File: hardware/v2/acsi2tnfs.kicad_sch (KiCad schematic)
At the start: 24 parts, among them J1 Debug, J2 To ACSI, J3 To SD card, J4 Debug Header, Q1 BC547, Q2 BC547, U1 SN74LVC245APW, U2 SN74LVC245APW

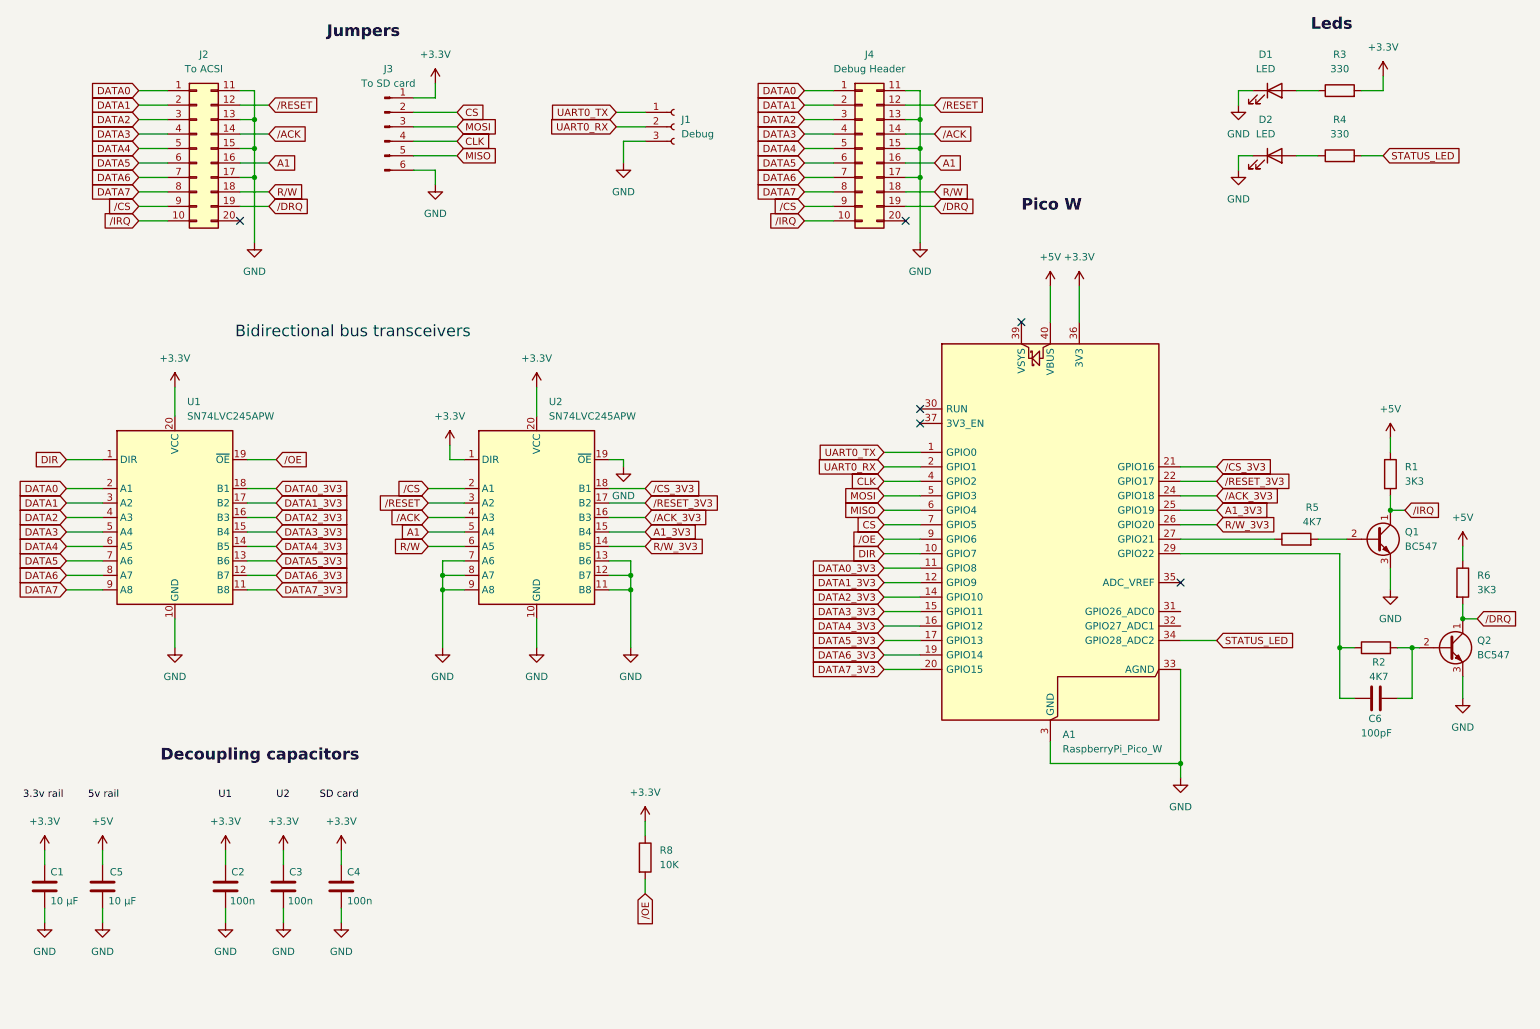
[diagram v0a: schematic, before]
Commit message: Hardware: v2 board (DB19 on the PCB, 74LS07, SD, button, leds) and dev schematic changes
Co-Authored-By: Claude Opus 5.5 <noreply@anthropic.com>
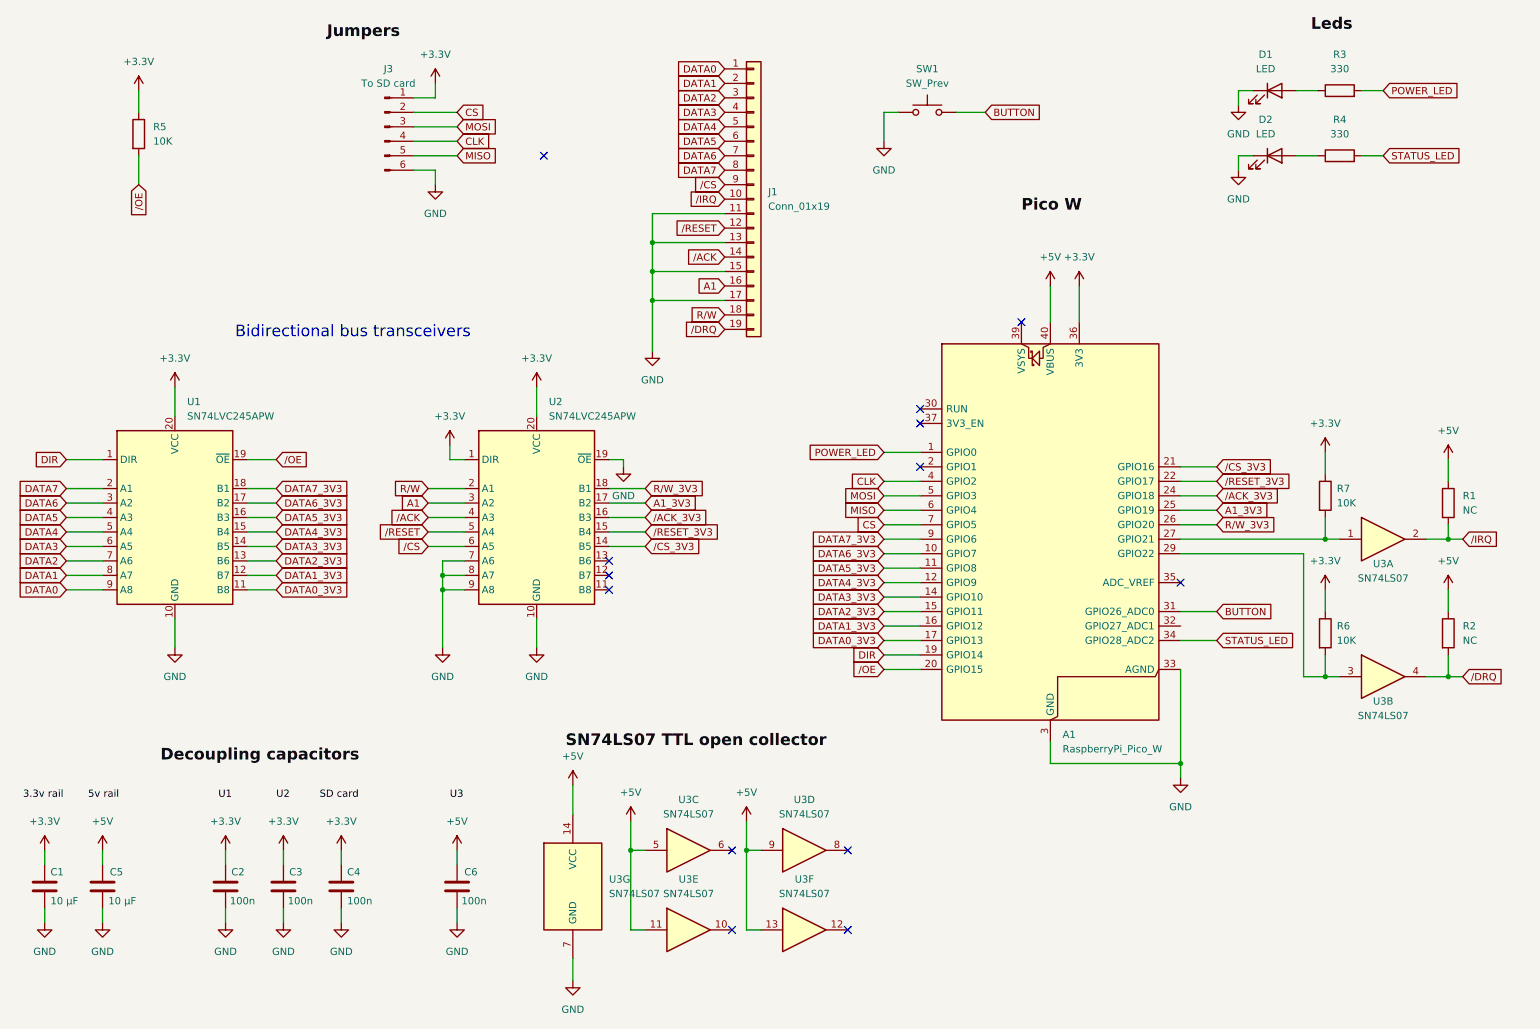
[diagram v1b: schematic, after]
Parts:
- removed J1: Debug, Connector_PinHeader_2.54mm:PinHeader_1x03_P2.54mm_Vertical, symbol Connector:Conn_01x03_Socket
- removed J2: To ACSI, Library:PinHeader_2x10_P2.54mm_Vertical_NR_PER_ROW, symbol Connector_Generic:Conn_02x10_Top_Bottom
- removed J4: Debug Header, Library:PinHeader_2x10_P2.54mm_Vertical_NR_PER_ROW, symbol Connector_Generic:Conn_02x10_Top_Bottom
- removed Q1, Q2: BC547, Package_TO_SOT_THT:TO-92_Inline, symbol Transistor_BJT:BC547
- removed R8: 10K, Resistor_SMD:R_0805_2012Metric, symbol Device:R
- added J1: Conn_01x19, ACSI Connector:ACSI_DB19_Male_WAGO_243-131, symbol Connector_Generic:Conn_01x19
- added R7: 10K, Resistor_SMD:R_0805_2012Metric, symbol Device:R
- added SW1: SW_Prev, Button_Switch_THT:SW_Tactile_SKHH_Angled, symbol Switch:SW_Push
- added U3: SN74LS07, Package_SO:SOIC-14_3.9x8.7mm_P1.27mm, symbol 74xx:SN74LS07
- C6: value 100pF -> 100n
- R1: value 3K3 -> NC
- R2: value 4K7 -> NC
- R5: value 4K7 -> 10K
- R6: value 3K3 -> 10K
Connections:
- net +3.3V: now also R5.1, R6.1, R7.1; no longer R3.2
- net +5V: now also C6.1, R2.1, U3.11, U3.13, U3.14 (VCC), U3.5, U3.9; no longer R6.1
- net A1: now also U2.3 (A2), J1.16 (Pin_16); no longer U2.5 (A4)
- net A1_3V3: now also U2.17 (B2); no longer U2.15 (B4)
- net DATA0: now also U1.9 (A8), J1.1 (Pin_1); no longer U1.2 (A1)
- net DATA0_3V3: now also A1.17 (GPIO13), U1.11 (B8); no longer A1.11 (GPIO8), U1.18 (B1)
- net DATA1: now also U1.8 (A7), J1.2 (Pin_2); no longer U1.3 (A2)
- net DATA1_3V3: now also A1.16 (GPIO12), U1.12 (B7); no longer A1.12 (GPIO9), U1.17 (B2)
- net DATA2: now also U1.7 (A6), J1.3 (Pin_3); no longer U1.4 (A3)
- net DATA2_3V3: now also A1.15 (GPIO11), U1.13 (B6); no longer A1.14 (GPIO10), U1.16 (B3)
- net DATA3: now also U1.6 (A5), J1.4 (Pin_4); no longer U1.5 (A4)
- net DATA3_3V3: now also A1.14 (GPIO10), U1.14 (B5); no longer A1.15 (GPIO11), U1.15 (B4)
- net DATA4: now also U1.5 (A4), J1.5 (Pin_5); no longer U1.6 (A5)
- net DATA4_3V3: now also A1.12 (GPIO9), U1.15 (B4); no longer A1.16 (GPIO12), U1.14 (B5)
- net DATA5: now also U1.4 (A3), J1.6 (Pin_6); no longer U1.7 (A6)
- net DATA5_3V3: now also A1.11 (GPIO8), U1.16 (B3); no longer A1.17 (GPIO13), U1.13 (B6)
- net DATA6: now also U1.3 (A2), J1.7 (Pin_7); no longer U1.8 (A7)
- net DATA6_3V3: now also A1.10 (GPIO7), U1.17 (B2); no longer A1.19 (GPIO14), U1.12 (B7)
- net DATA7: now also U1.2 (A1), J1.8 (Pin_8); no longer U1.9 (A8)
- net DATA7_3V3: now also A1.9 (GPIO6), U1.18 (B1); no longer A1.20 (GPIO15), U1.11 (B8)
- net DIR: now also A1.19 (GPIO14); no longer A1.10 (GPIO7)
- net GND: now also C6.2, J1.11 (Pin_11), J1.13 (Pin_13), J1.15 (Pin_15), J1.17 (Pin_17), SW1.1, U3.7 (GND); no longer U2.11 (B8), U2.12 (B7), U2.13 (B6)
- net R/W: now also U2.2 (A1), J1.18 (Pin_18); no longer U2.6 (A5)
- net R/W_3V3: now also U2.18 (B1); no longer U2.14 (B5)
- net /ACK: now also J1.14 (Pin_14)
- net /CS: now also U2.6 (A5), J1.9 (Pin_9); no longer U2.2 (A1)
- net /CS_3V3: now also U2.14 (B5); no longer U2.18 (B1)
- net /DRQ: now also R2.2, J1.19 (Pin_19), U3.4; no longer R6.2
- net /IRQ: now also J1.10 (Pin_10), U3.2
- net /OE: now also A1.20 (GPIO15), R5.2; no longer A1.9 (GPIO6)
- net /RESET: now also U2.5 (A4), J1.12 (Pin_12); no longer U2.3 (A2)
- net /RESET_3V3: now also U2.15 (B4); no longer U2.17 (B2)
- net at A1.27 (GPIO21): now also R7.2, U3.1; no longer R5.1
- net BUTTON: now reaches A1.31 (GPIO26_ADC0)
- net BUTTON: now also SW1.2
- net UART0_RX: no longer names the net of A1.2 (GPIO1)
- net UART0_TX renamed POWER_LED
- net POWER_LED: now also R3.2
- new net: A1.29 (GPIO22), R6.2, U3.3
- no-connect marks 6 -> 13
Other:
- moved on the sheet: R1

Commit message: Hardware: v2 and v2-cable, drop v1 and dev
v2 (DB19 on the board) and the new v2-cable (flat cable to a Lotharek DB19
adapter, pass-through header) share one circuit: 74LS07 for /IRQ and /DRQ,
pull-ups on /OE and the 74LS07 inputs, no pull-ups on /IRQ and /DRQ (those
upset the floppy drive when the board is off). v2-cable's box headers are
numbered per row, so pin n is ACSI pin n like on the adapter. Each project
carries its own footprints and fp-lib-table. hardware/README.md explains
both boards. v1, dev and the old gerbers are gone.

Co-Authored-By: Claude Opus 5.5 <noreply@anthropic.com>
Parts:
- removed R1, R2: NC, Resistor_SMD:R_0805_2012Metric, symbol Device:R
- J1: value Conn_01x19 -> To ACSI
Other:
- note added: "3.3v rail"
- note added: "5v rail"
- note added: "ACSI connector (DB19)"
- note added: "Decoupling capacitors"
- note added: "Enable/disable button"
- note added: "Leds"
- note added: "Micro SD card"
- note added: "Optional Micro SD card"
- note added: "Pico W"
- note added: "Pull up"
- note added: "SN74LS07 TTL open collector"
- note added: "U1"
- note added: "U2"
- note added: "U3"
- moved on the sheet: A1, C1, C2, C3, C4, C5, C6, D1, D2, J1, J3, R3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

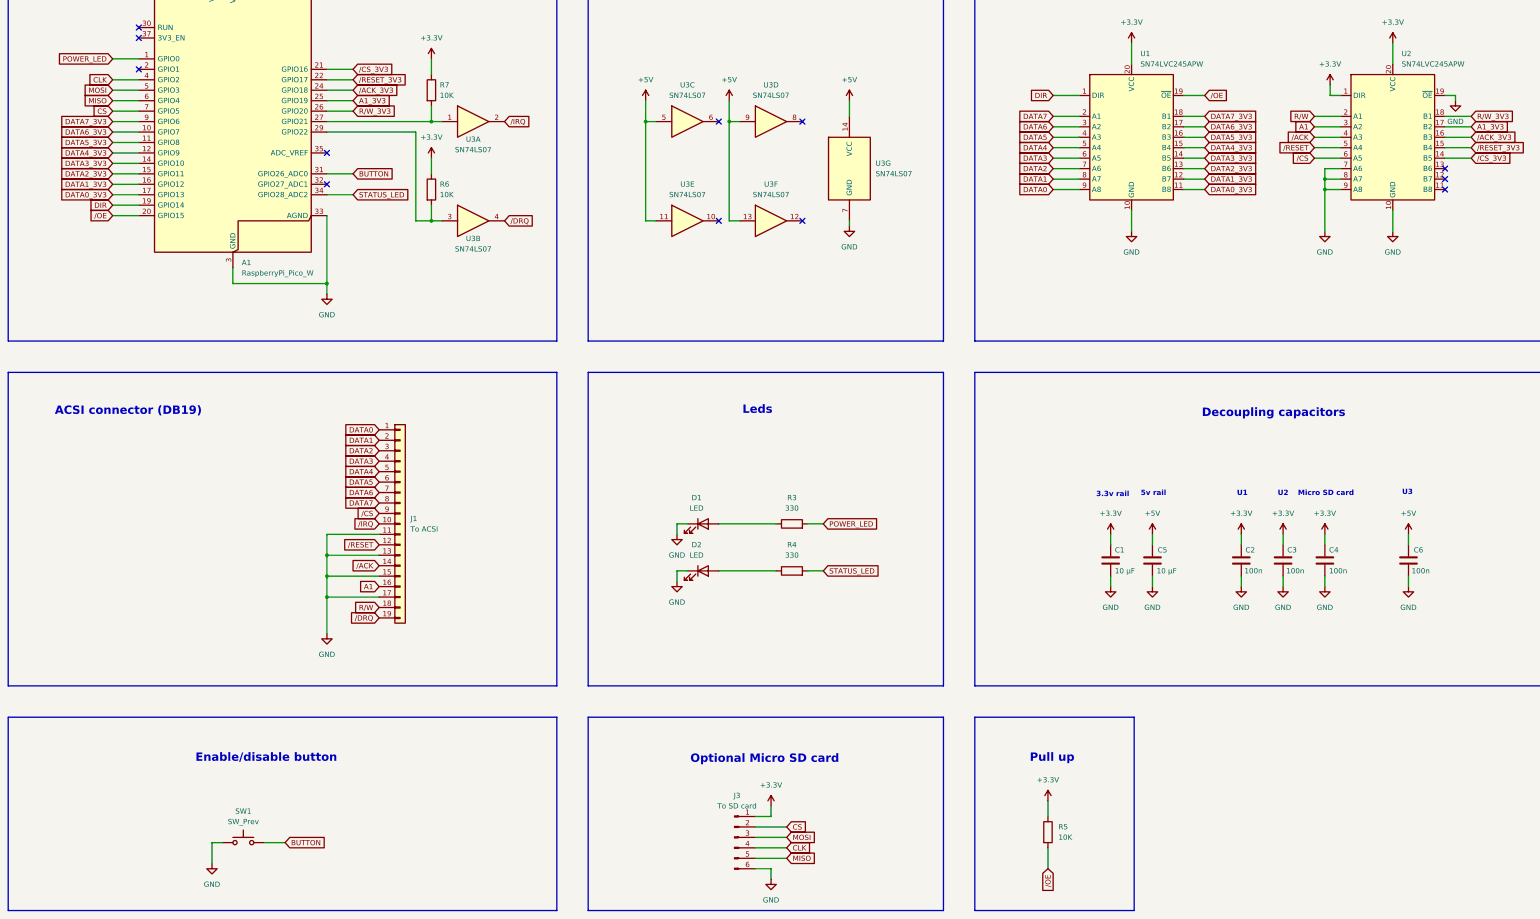
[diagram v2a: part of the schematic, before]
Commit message: hardware/v2: TF-01A micro SD socket on the board, improved layout
Card1 uses the footprint from the project library; schema.pdf updated.

Co-Authored-By: Claude Opus 5.5 <noreply@anthropic.com>
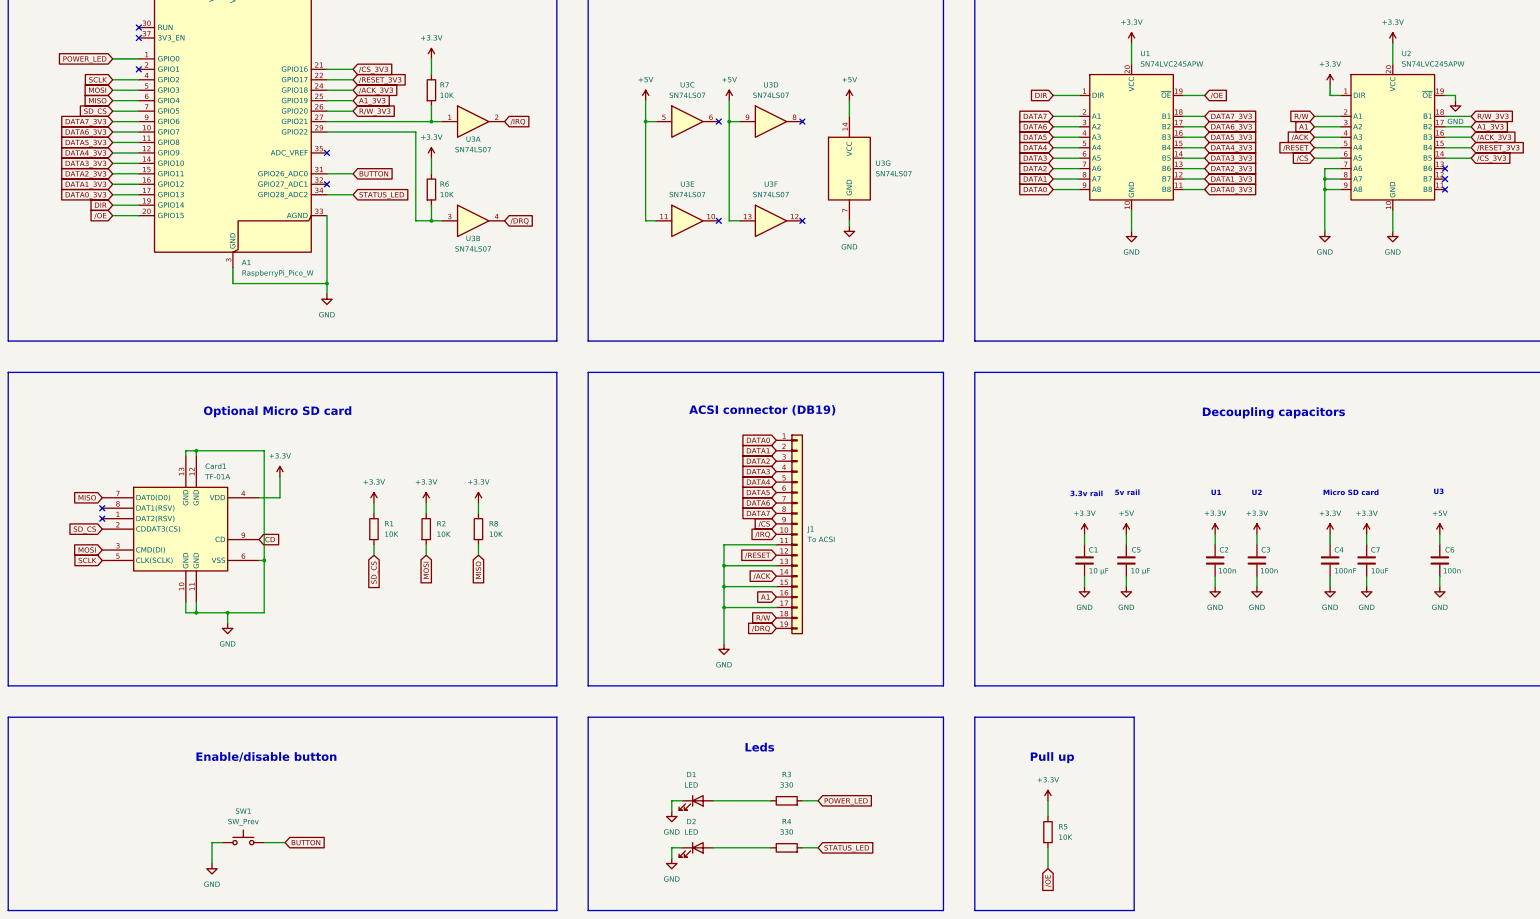
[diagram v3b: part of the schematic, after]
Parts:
- removed J3: To SD card, Connector_PinHeader_2.54mm:PinHeader_1x06_P2.54mm_Vertical, symbol Connector:Conn_01x06_Pin
- added C7: 10uF, Capacitor_SMD:C_0805_2012Metric, symbol Device:C
- added Card1: TF-01A, ACSI Connector:TF-SMD_TF-01A, symbol Micro SD card holder:TF-01A
- added R1, R2, R8: 10K, Resistor_SMD:R_0805_2012Metric, symbol Device:R
- C4: value 100n -> 100nF
- D1, D2: footprint LED_SMD:LED_0805_2012Metric -> LED_THT:LED_D3.0mm
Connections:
- net +3.3V: now also C7.1, Card1.4 (VDD), R1.1, R2.1, R8.1
- net GND: now also C7.2, Card1.10 (GND), Card1.11 (GND), Card1.12 (GND), Card1.13 (GND), Card1.6 (VSS)
- net MISO: now also Card1.7 (DAT0(D0)), R8.2
- net MOSI: now also Card1.3 (CMD(DI)), R2.2
- net CLK renamed SCLK
- net SCLK: now also Card1.5 (CLK(SCLK))
- net CS renamed SD_CS
- net SD_CS: now also Card1.2 (CDDAT3(CS)), R1.2
- new net CD: Card1.9 (CD)
- no-connect marks 13 -> 15
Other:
- moved on the sheet: C1, C2, C3, C5, C6, D1, D2, J1, R3, R4

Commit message: hardware: U1/U2 are 74LVC245ADW, silkscreen says ACSI
Both boards: the value of U1/U2 matches the SOIC-20W footprint, the
silkscreen text reads ACSI instead of ASCI, and a stray text outside the
v2 board is gone. schema.pdf and the 3D views updated.

Co-Authored-By: Claude Opus 5.5 <noreply@anthropic.com>
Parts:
- U1, U2: value SN74LVC245APW -> 74LVC245ADW
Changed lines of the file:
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@@
 			)
 		)
-		(property "Value" "SN74LVC245APW"
+		(property "Value" "74LVC245ADW"
 			(at 295.5133 71.12 0)
 			(effects
@@
 			)
 		)
-		(property "Value" "SN74LVC245APW"
+		(property "Value" "74LVC245ADW"
 			(at 359.0133 71.12 0)
 			(effects

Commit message: hardware: D1 yellow, D2 blue, both on 470 ohm
R3 and R4 are 470 ohm in both boards; the led values name the colour
(v2-cable: D3 yellow, D4 blue as well). schema.pdf and the parts list
updated.

Co-Authored-By: Claude Opus 5.5 <noreply@anthropic.com>
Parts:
- D1: value LED -> LED yellow
- D2: value LED -> LED blue
- R3, R4: value 330 -> 470
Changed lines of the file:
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@@
 			)
 		)
-		(property "Value" "LED"
+		(property "Value" "LED blue"
 			(at 186.3725 257.81 0)
 			(effects
@@
 			)
 		)
-		(property "Value" "LED"
+		(property "Value" "LED yellow"
 			(at 186.3725 246.38 0)
 			(effects
@@
 			)
 		)
-		(property "Value" "330"
+		(property "Value" "470"
 			(at 209.55 246.38 90)
 			(effects
@@
 			)
 		)
-		(property "Value" "330"
+		(property "Value" "470"
 			(at 209.55 257.81 90)
 			(effects
